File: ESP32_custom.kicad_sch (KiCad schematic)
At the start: 29 parts, among them J1 TYPE-C-31-M-12, J2 Conn_01x13_Pin, J3 Conn_01x13_Pin, SW1 SW_Push, SW2 SW_Push, U1 ESP32-S3-WROOM-1, U4 AMS1117-3.3

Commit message: update pcb
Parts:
- removed D6: D_Schottky_Dual_Series_AKC_Split, Diode_SMD:D_0201_0603Metric, symbol Device:D_Schottky_Dual_Series_AKC_Split
- added D4: 1N5819HW-7-F, ul_1N5819HW-7-F:1N5819HW-7-F_DIO, symbol Device:D_Schottky_Dual_CommonAnode_AKK_Split
- D1, D2, D3: footprint LESD5D5.0CT1G:TVS_LESD5D5.0CT1G -> LESD5D:TVS_LESD5D5.0CT1G
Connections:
- net +5V: now also D4.2 (K)
- net VBUS: now also D4.1 (A)
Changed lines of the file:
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@@
 			)
 		)
-		(property "Footprint" "LESD5D5.0CT1G:TVS_LESD5D5.0CT1G"
+		(property "Footprint" "LESD5D:TVS_LESD5D5.0CT1G"
 			(at 240.03 55.88 0)
 			(hide yes)
@@
 			)
 		)
-		(property "Footprint" "LESD5D5.0CT1G:TVS_LESD5D5.0CT1G"
+		(property "Footprint" "LESD5D:TVS_LESD5D5.0CT1G"
 			(at 246.38 55.88 0)
 			(hide yes)
@@
 			)
 		)
-		(property "Footprint" "LESD5D5.0CT1G:TVS_LESD5D5.0CT1G"
+		(property "Footprint" "LESD5D:TVS_LESD5D5.0CT1G"
 			(at 252.73 55.88 0)
 			(hide yes)
@@
 	)
 	(symbol
-		(lib_id "Device:D_Schottky_Dual_Series_AKC_Split")
-		(at 250.19 35.56 0)
+		(lib_id "power:VCC")
+		(at 34.29 58.42 0)
 		(unit 1)
 		(body_style 1)
@@
 		(dnp no)
 		(fields_autoplaced yes)
-		(property "Reference" "D6"
-			(at 250.444 29.21 0)
+		(property "Reference" "#PWR021"
+			(at 34.29 62.23 0)
+			(hide yes)
 			(show_name no)
 			(do_not_autoplace no)
@@
 			)
 		)
-		(property "Value" "D_Schottky_Dual_Series_AKC_Split"
-			(at 250.444 31.75 0)
+		(property "Value" "VCC"
+			(at 34.29 53.34 0)
 			(show_name no)
 			(do_not_autoplace no)
@@
 			)
 		)
-		(property "Footprint" "Diode_SMD:D_0201_0603Metric"
-			(at 247.65 38.1 0)
+		(property "Footprint" ""
+			(at 34.29 58.42 0)
 			(hide yes)
 			(show_name no)
@@
 		)
 		(property "Datasheet" ""
-			(at 247.65 38.1 0)
+			(at 34.29 58.42 0)
 			(hide yes)
 			(show_name no)
@@
 			)
 		)
-		(property "Description" "Dual Schottky diode, anode/cathode/center"
-			(at 250.19 35.56 0)
+		(property "Description" "Power symbol creates a global label with name \"VCC\""
+			(at 34.29 58.42 0)
 			(hide yes)
 			(show_name no)
@@
 			)
 		)
-		(pin "2"
-		)
 		(pin "1"
 		)
-		(pin "3"
-		)
 		(instances
 			(project "ESP32_custom"
 				(path "/d69a2644-c978-49ae-b7c7-18eba523ada2"
-					(reference "D6")
+					(reference "#PWR021")
 					(unit 1)
 				)
@@
 	)
 	(symbol
-		(lib_id "power:VCC")
-		(at 34.29 58.42 0)
+		(lib_id "Switch:SW_Push")
+		(at 52.07 43.18 0)
 		(unit 1)
 		(body_style 1)
@@
 		(dnp no)
 		(fields_autoplaced yes)
-		(property "Reference" "#PWR021"
-			(at 34.29 62.23 0)
-			(hide yes)
+		(property "Reference" "SW1"
+			(at 52.07 35.56 0)
 			(show_name no)
 			(do_not_autoplace no)
@@
 			)
 		)
-		(property "Value" "VCC"
-			(at 34.29 53.34 0)
+		(property "Value" "SW_Push"
+			(at 52.07 38.1 0)
 			(show_name no)
 			(do_not_autoplace no)
@@
 			)
 		)
-		(property "Footprint" ""
-			(at 34.29 58.42 0)
+		(property "Footprint" "Button_Switch_SMD:SW_SPST_B3U-1000P"
+			(at 52.07 38.1 0)
 			(hide yes)
 			(show_name no)
@@
 		)
 		(property "Datasheet" ""
-			(at 34.29 58.42 0)
+			(at 52.07 38.1 0)
 			(hide yes)
 			(show_name no)
@@
 			)
 		)
-		(property "Description" "Power symbol creates a global label with name \"VCC\""
-			(at 34.29 58.42 0)
+		(property "Description" "Push button switch, generic, two pins"
+			(at 52.07 43.18 0)
 			(hide yes)
 			(show_name no)
@@
 			)
 		)
+		(pin "2"
+		)
 		(pin "1"
 		)
@@
 			(project "ESP32_custom"
 				(path "/d69a2644-c978-49ae-b7c7-18eba523ada2"
-					(reference "#PWR021")
+					(reference "SW1")
 					(unit 1)
 				)
@@
 	)
 	(symbol
-		(lib_id "Switch:SW_Push")
-		(at 52.07 43.18 0)
+		(lib_id "power:PWR_FLAG")
+		(at 41.91 128.27 0)
 		(unit 1)
 		(body_style 1)
@@
 		(dnp no)
 		(fields_autoplaced yes)
-		(property "Reference" "SW1"
-			(at 52.07 35.56 0)
+		(property "Reference" "#FLG01"
+			(at 41.91 126.365 0)
+			(hide yes)
 			(show_name no)
 			(do_not_autoplace no)
@@
 			)
 		)
-		(property "Value" "SW_Push"
-			(at 52.07 38.1 0)
+		(property "Value" "PWR_FLAG"
+			(at 41.91 123.19 0)
 			(show_name no)
 			(do_not_autoplace no)
@@
 			)
 		)
-		(property "Footprint" "Button_Switch_SMD:SW_SPST_B3U-1000P"
-			(at 52.07 38.1 0)
+		(property "Footprint" ""
+			(at 41.91 128.27 0)
 			(hide yes)
 			(show_name no)
@@
 		)
 		(property "Datasheet" ""
-			(at 52.07 38.1 0)
+			(at 41.91 128.27 0)
 			(hide yes)
 			(show_name no)
@@
 			)
 		)
-		(property "Description" "Push button switch, generic, two pins"
-			(at 52.07 43.18 0)
+		(property "Description" "Special symbol for telling ERC where power comes from"
+			(at 41.91 128.27 0)
 			(hide yes)
 			(show_name no)
@@
 			)
 		)
-		(pin "2"
-		)
 		(pin "1"
 		)
@@
 			(project "ESP32_custom"
 				(path "/d69a2644-c978-49ae-b7c7-18eba523ada2"
-					(reference "SW1")
+					(reference "#FLG01")
 					(unit 1)
 				)
@@
 	)
 	(symbol
-		(lib_id "power:PWR_FLAG")
-		(at 41.91 128.27 0)
+		(lib_id "Device:D_Schottky_Dual_CommonAnode_AKK_Split")
+		(at 250.19 35.56 0)
 		(unit 1)
 		(body_style 1)
@@
 		(dnp no)
 		(fields_autoplaced yes)
-		(property "Reference" "#FLG01"
-			(at 41.91 126.365 0)
-			(hide yes)
+		(property "Reference" "D4"
+			(at 250.444 29.21 0)
 			(show_name no)
 			(do_not_autoplace no)
@@
 			)
 		)
-		(property "Value" "PWR_FLAG"
-			(at 41.91 123.19 0)
+		(property "Value" "1N5819HW-7-F"
+			(at 250.444 31.75 0)
 			(show_name no)
 			(do_not_autoplace no)
@@
 			)
 		)
-		(property "Footprint" ""
-			(at 41.91 128.27 0)
+		(property "Footprint" "ul_1N5819HW-7-F:1N5819HW-7-F_DIO"
+			(at 247.65 38.1 0)
 			(hide yes)
 			(show_name no)
@@
 		)
 		(property "Datasheet" ""
-			(at 41.91 128.27 0)
+			(at 247.65 38.1 0)
 			(hide yes)
 			(show_name no)
@@
 			)
 		)
-		(property "Description" "Special symbol for telling ERC where power comes from"
-			(at 41.91 128.27 0)
+		(property "Description" "Dual Schottky diode, common anode on pin 1"
+			(at 250.19 35.56 0)
 			(hide yes)
 			(show_name no)
@@
 			)
 		)
+		(pin "3"
+		)
+		(pin "2"
+		)
 		(pin "1"
 		)
@@
 			(project "ESP32_custom"
 				(path "/d69a2644-c978-49ae-b7c7-18eba523ada2"
-					(reference "#FLG01")
+					(reference "D4")
 					(unit 1)
 				)

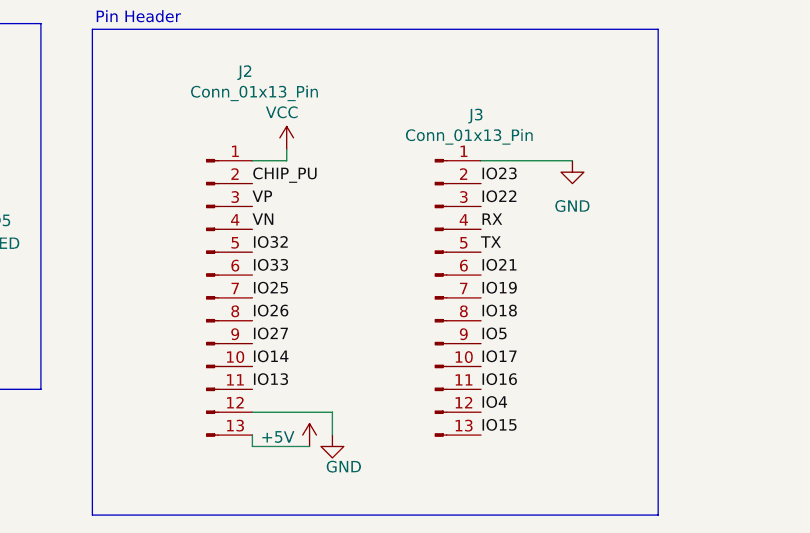
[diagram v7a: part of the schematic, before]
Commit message: arrange components and update pin header label
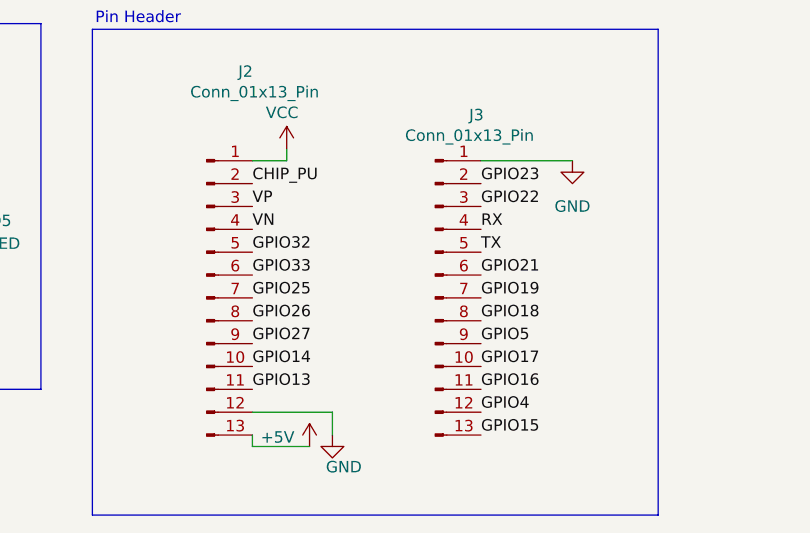
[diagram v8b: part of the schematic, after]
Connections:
- net IO13 is gone; now on net GPIO13: J2.11 (Pin_11)
- net IO14 is gone; now on net GPIO14: J2.10 (Pin_10)
- net IO15 is gone; now on net GPIO15: J3.13 (Pin_13)
- net IO16 is gone; now on net GPIO16: J3.11 (Pin_11)
- net IO17 is gone; now on net GPIO17: J3.10 (Pin_10)
- net IO18 is gone; now on net GPIO18: J3.8 (Pin_8)
- net IO19 is gone; now on net D-: J3.7 (Pin_7)
- net IO21 is gone; now on net GPIO21: J3.6 (Pin_6)
- net IO22 renamed GPIO22
- net IO23 renamed GPIO23
- net IO25 renamed GPIO25
- net IO26 renamed GPIO26
- net IO27 renamed GPIO27
- net IO32 renamed GPIO32
- net IO33 renamed GPIO33
- net IO4 renamed GPIO4
- net IO5 renamed GPIO5
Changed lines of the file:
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@@
 		)
 	)
-	(label "IO16"
+	(label "GPIO16"
 		(at 152.4 156.21 0)
 		(effects
@@
 		)
 	)
-	(label "IO13"
+	(label "GPIO13"
 		(at 127 156.21 0)
 		(effects
@@
 		)
 	)
-	(label "IO4"
+	(label "GPIO4"
 		(at 152.4 158.75 0)
 		(effects
@@
 		)
 	)
-	(label "IO27"
+	(label "GPIO27"
 		(at 127 151.13 0)
 		(effects
@@
 		)
 	)
-	(label "IO25"
+	(label "GPIO25"
 		(at 127 146.05 0)
 		(effects
@@
 		)
 	)
-	(label "IO19"
+	(label "GPIO19"
 		(at 152.4 146.05 0)
 		(effects
@@
 		)
 	)
-	(label "IO17"
+	(label "GPIO17"
 		(at 152.4 153.67 0)
 		(effects
@@
 		)
 	)
-	(label "IO22"
+	(label "GPIO22"
 		(at 152.4 135.89 0)
 		(effects
@@
 		)
 	)
-	(label "IO26"
+	(label "GPIO26"
 		(at 127 148.59 0)
 		(effects
@@
 		)
 	)
-	(label "IO23"
+	(label "GPIO23"
 		(at 152.4 133.35 0)
 		(effects
@@
 		)
 	)
-	(label "IO33"
+	(label "GPIO33"
 		(at 127 143.51 0)
 		(effects
@@
 		)
 	)
-	(label "IO21"
+	(label "GPIO21"
 		(at 152.4 143.51 0)
 		(effects
@@
 		)
 	)
-	(label "IO18"
+	(label "GPIO18"
 		(at 152.4 148.59 0)
 		(effects
@@
 		)
 	)
-	(label "IO5"
+	(label "GPIO5"
 		(at 152.4 151.13 0)
 		(effects
@@
 		)
 	)
-	(label "IO32"
+	(label "GPIO32"
 		(at 127 140.97 0)
 		(effects
@@
 		)
 	)
-	(label "IO14"
+	(label "GPIO14"
 		(at 127 153.67 0)
 		(effects
@@
 		)
 	)
-	(label "IO15"
+	(label "GPIO15"
 		(at 152.4 161.29 0)
 		(effects
